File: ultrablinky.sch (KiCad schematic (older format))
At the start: 126 parts, among them J1 DNP, J2 SJ1-3523N, J3 SJ1-3523N, J4 Barrel_Jack_5.5x2.5, J5 DNP, J6 DNP, J7 Terminal5, J8 SJ1-3523N, Q1 DMP6180SK3Q-13, Q2 DMP6180SK3Q-13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

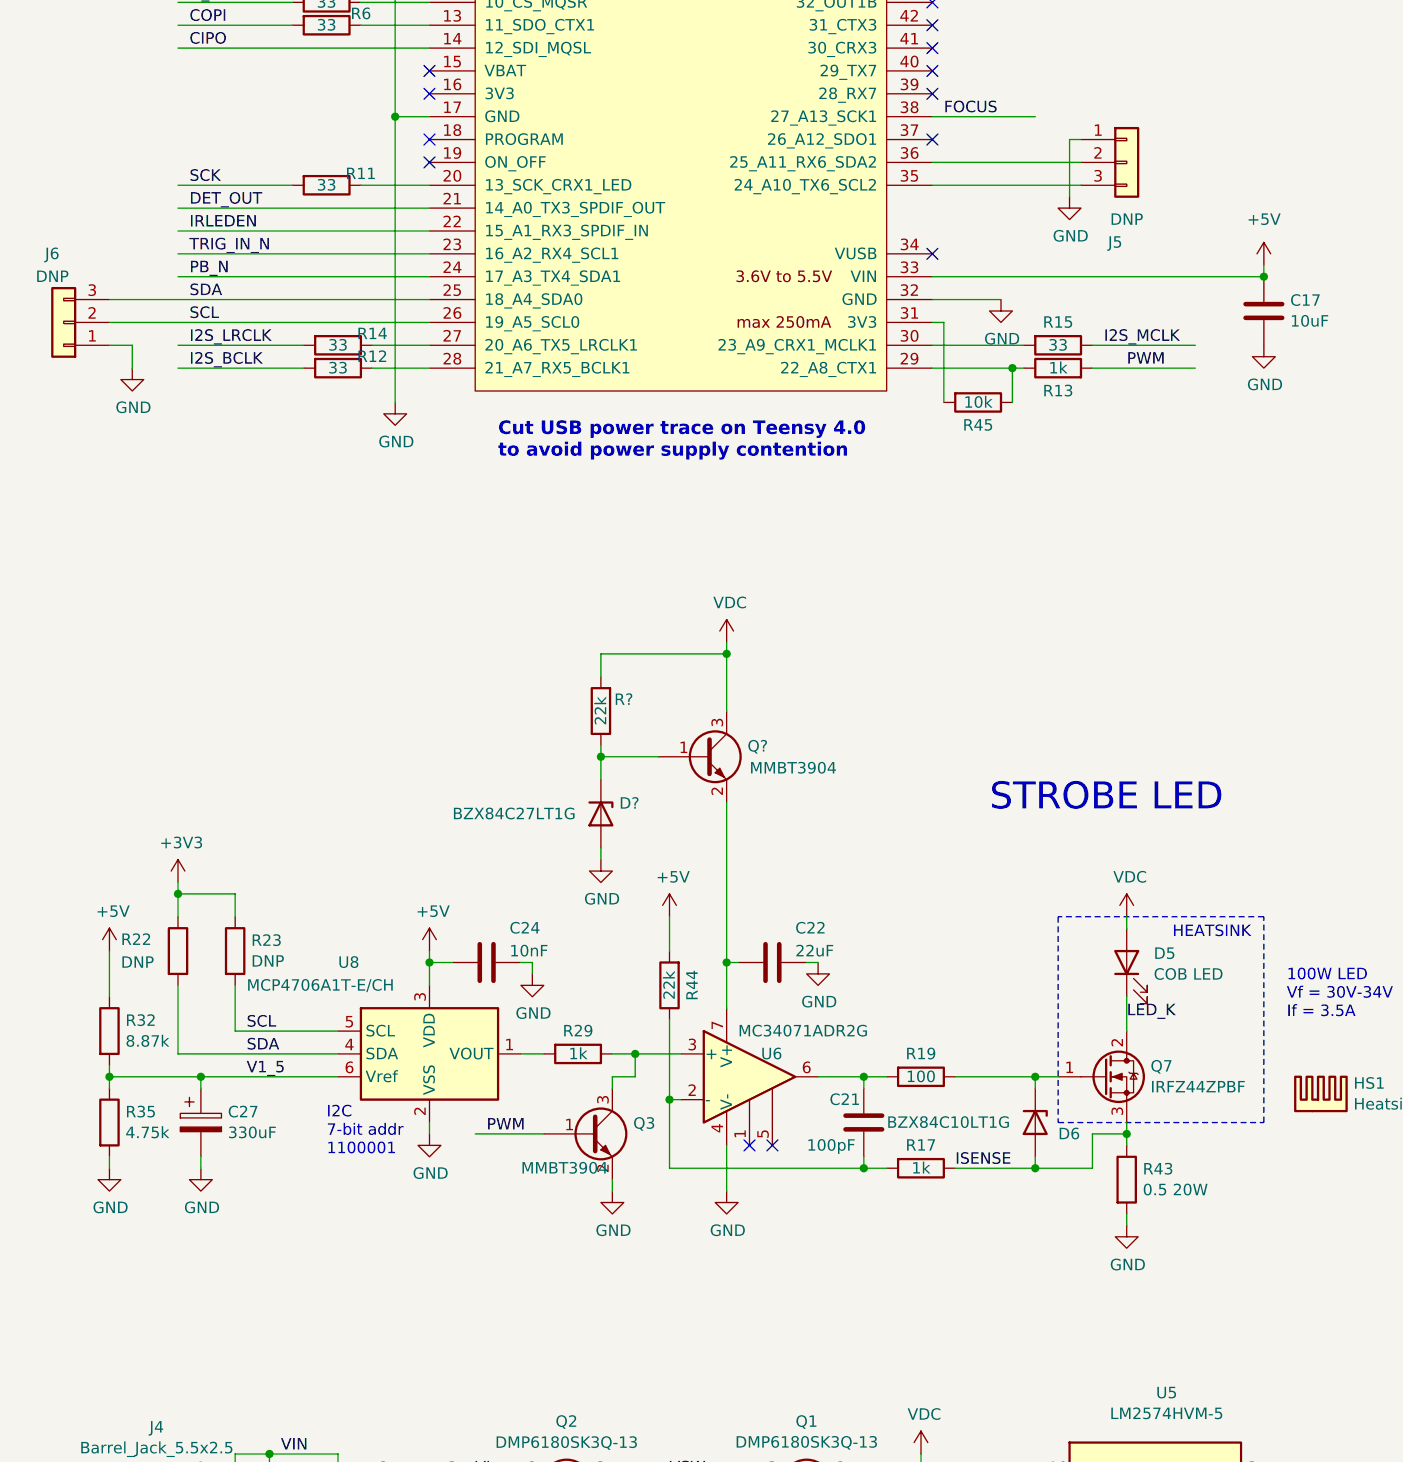
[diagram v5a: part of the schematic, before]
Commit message: Changed current-sense resistor to allow higher current
The current-sense resistor R43 was changed from 0.5-ohm to 0.05-ohm to
allow more current while keeping the voltage across the resistor lower.
Additionally, a pull-down resistor was added to the op amp non-inverting
input so that a current-sense voltage of 0V to 12V gets converted to a
range of 0.2V to 4.9V at the non-inverting input of the op amp.

Additionally, the voltage divider on the Vref input of the MCP4706A DAC
was removed because the VDD power input will be used as the reference
instead.
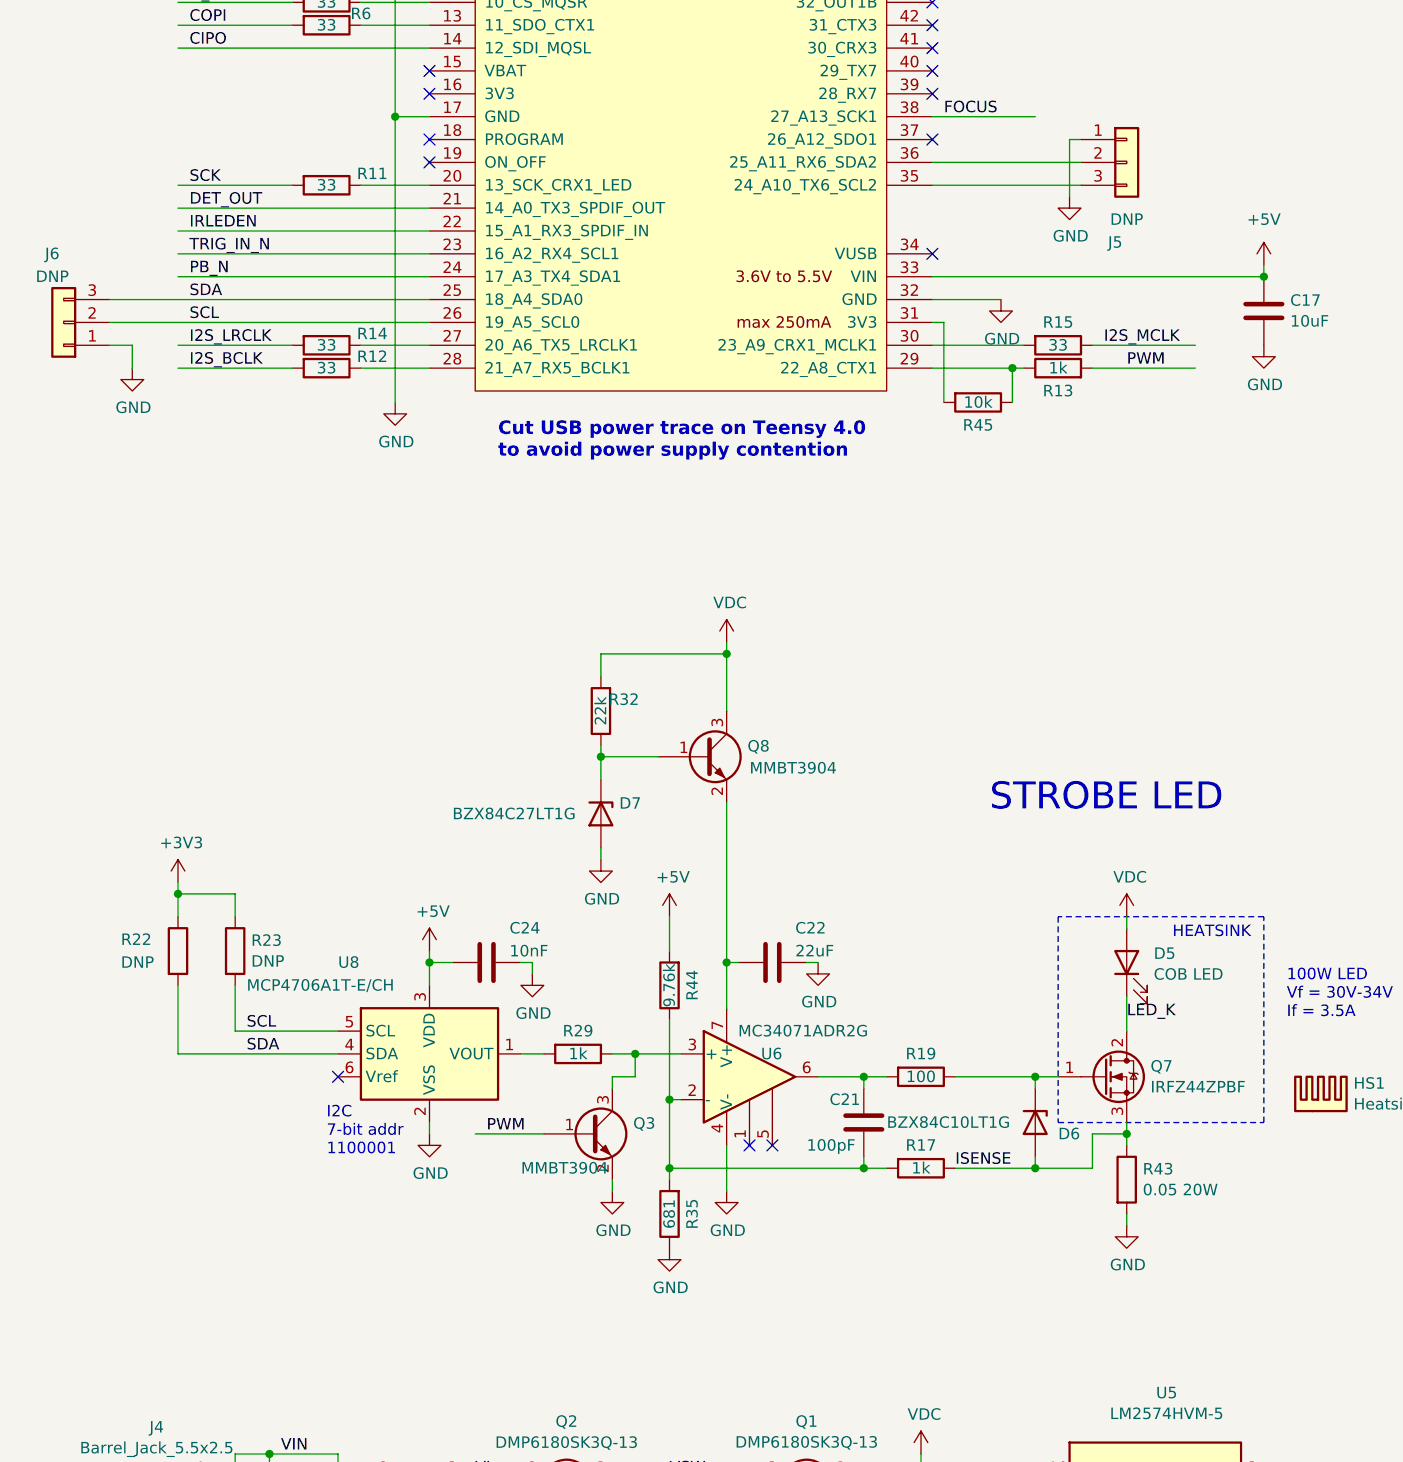
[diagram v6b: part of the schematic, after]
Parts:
- removed C27: 330uF, Capacitor_SMD:CP_Elec_8x10, symbol Device:CP
- removed R32: 8.87k, Resistor_SMD:R_0805_2012Metric, symbol Device:R
- R35: value 4.75k -> 681; Source Mouser 603-RC0805FR-074K75P -> Mouser 603-RC0805FR-07681RL
- R43: value 0.5 20W -> 0.05 20W; Source Mouser 652-PWR220T-20-R500F -> Mouser 652-PWR220T-20-R050J
- R44: value 22k -> 9.76k; Source Mouser 603-RC0805JR-0722KL -> Mouser 603-RC0805FR-079K76L
- gave numbers to parts that had none: 3
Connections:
- net labels removed: V1_5
- wire segments 387 -> 380
- no-connect marks 23 -> 24
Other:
- moved on the sheet: R12, R14
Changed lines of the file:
@@
 P 5450 7200
 F 0 "R43" H 5520 7246 50  0000 L CNN
-F 1 "0.5 20W" H 5520 7155 50  0000 L CNN
+F 1 "0.05 20W" H 5520 7155 50  0000 L CNN
 F 2 "Package_TO_SOT_THT:TO-220-2_Horizontal_TabDown" V 5380 7200 50  0001 C CNN
 F 3 "~" H 5450 7200 50  0001 C CNN
-F 4 "Mouser 652-PWR220T-20-R500F" H 5450 7200 50  0001 C CNN "Source"
+F 4 "Mouser 652-PWR220T-20-R050J" H 5450 7200 50  0001 C CNN "Source"
 	1    5450 7200
 	1    0    0    -1
@@
 Wire Wire Line
 	5750 3650 5300 3650
-Text Label 1600 6750 0    50   ~ 0
-V1_5
 $Comp
 L 0_my_symbols:LM2574HVM-5 U5
@@
 U 1 1 603CBFD5
 P 1950 2850
-F 0 "R11" V 1900 3000 50  0000 C CNN
+F 0 "R11" V 1900 3050 50  0000 C CNN
 F 1 "33" V 1950 2850 50  0000 C CNN
 F 2 "Resistor_SMD:R_0805_2012Metric" V 1880 2850 50  0001 C CNN
@@
 	1    0    0    -1
 $EndComp
-$Comp
-L Device:R R35
-U 1 1 6032F8D7
-P 1000 6950
-F 0 "R35" H 1070 6996 50  0000 L CNN
-F 1 "4.75k" H 1070 6905 50  0000 L CNN
-F 2 "Resistor_SMD:R_0805_2012Metric" V 930 6950 50  0001 C CNN
-F 3 "~" H 1000 6950 50  0001 C CNN
-F 4 "Mouser 603-RC0805FR-074K75P" H 1000 6950 50  0001 C CNN "Source"
-	1    1000 6950
-	1    0    0    -1
-$EndComp
-$Comp
-L Device:R R32
-U 1 1 60330655
-P 1000 6550
-F 0 "R32" H 1070 6596 50  0000 L CNN
-F 1 "8.87k" H 1070 6505 50  0000 L CNN
-F 2 "Resistor_SMD:R_0805_2012Metric" V 930 6550 50  0001 C CNN
-F 3 "~" H 1000 6550 50  0001 C CNN
-F 4 "Mouser 603-RT0805FRE078K87L" H 1000 6550 50  0001 C CNN "Source"
-	1    1000 6550
-	1    0    0    -1
-$EndComp
-$Comp
-L power:GND #PWR0126
-U 1 1 6034CF10
-P 1000 7150
-F 0 "#PWR0126" H 1000 6900 50  0001 C CNN
-F 1 "GND" H 1005 6977 50  0000 C CNN
-F 2 "" H 1000 7150 50  0001 C CNN
-F 3 "" H 1000 7150 50  0001 C CNN
-	1    1000 7150
-	1    0    0    -1
-$EndComp
-Wire Wire Line
-	1000 7100 1000 7150
-Wire Wire Line
-	1000 6800 1000 6750
-Wire Wire Line
-	1000 6700 1000 6750
-Connection ~ 1000 6750
-Wire Wire Line
-	1000 6750 1400 6750
-$Comp
-L power:+5V #PWR0127
-U 1 1 60374662
-P 1000 6200
-F 0 "#PWR0127" H 1000 6050 50  0001 C CNN
-F 1 "+5V" H 1015 6373 50  0000 C CNN
-F 2 "" H 1000 6200 50  0001 C CNN
-F 3 "" H 1000 6200 50  0001 C CNN
-	1    1000 6200
-	1    0    0    -1
-$EndComp
-Wire Wire Line
-	1000 6200 1000 6400
-Wire Wire Line
-	1400 6800 1400 6750
-Connection ~ 1400 6750
-Wire Wire Line
-	1400 6750 2000 6750
-Wire Wire Line
-	1400 7100 1400 7150
-$Comp
-L power:GND #PWR0128
-U 1 1 6039BB5E
-P 1400 7150
-F 0 "#PWR0128" H 1400 6900 50  0001 C CNN
-F 1 "GND" H 1405 6977 50  0000 C CNN
-F 2 "" H 1400 7150 50  0001 C CNN
-F 3 "" H 1400 7150 50  0001 C CNN
-	1    1400 7150
-	1    0    0    -1
-$EndComp
 Text Notes 8000 10350 0    59   ~ 0
 Licensed under CERN-OHL-P v2
@@
 ENCB
 $Comp
-L Device:CP C27
-U 1 1 60454D8D
-P 1400 6950
-F 0 "C27" H 1518 6996 50  0000 L CNN
-F 1 "330uF" H 1518 6905 50  0000 L CNN
-F 2 "Capacitor_SMD:CP_Elec_8x10" H 1438 6800 50  0001 C CNN
-F 3 "~" H 1400 6950 50  0001 C CNN
-F 4 "Mouser 647-UUD1A331MNL" H 1400 6950 50  0001 C CNN "Source"
-	1    1400 6950
-	1    0    0    -1
-$EndComp
-$Comp
 L Device:R R24
 U 1 1 60484532
@@
 	1300 1750 1800 1750
 Wire Wire Line
-	1300 3650 1850 3650
+	1300 3650 1800 3650
 Wire Wire Line
-	1300 3550 1850 3550
+	1300 3550 1800 3550
 Wire Wire Line
 	4600 3550 5000 3550
@@
 L Device:R R12
 U 1 1 60B12468
-P 2000 3650
-F 0 "R12" V 1950 3800 50  0000 C CNN
-F 1 "33" V 2000 3650 50  0000 C CNN
-F 2 "Resistor_SMD:R_0805_2012Metric" V 1930 3650 50  0001 C CNN
-F 3 "~" H 2000 3650 50  0001 C CNN
-F 4 "Mouser 603-RC0805JR-1333RL" H 2000 3650 50  0001 C CNN "Source"
-	1    2000 3650
+P 1950 3650
+F 0 "R12" V 1900 3850 50  0000 C CNN
+F 1 "33" V 1950 3650 50  0000 C CNN
+F 2 "Resistor_SMD:R_0805_2012Metric" V 1880 3650 50  0001 C CNN
+F 3 "~" H 1950 3650 50  0001 C CNN
+F 4 "Mouser 603-RC0805JR-1333RL" H 1950 3650 50  0001 C CNN "Source"
+	1    1950 3650
 	0    1    1    0
 $EndComp
 Wire Wire Line
-	2150 3650 2400 3650
+	2100 3650 2400 3650
 $Comp
 L Device:R R14
 U 1 1 60B12D4F
-P 2000 3550
-F 0 "R14" V 1950 3700 50  0000 C CNN
-F 1 "33" V 2000 3550 50  0000 C CNN
-F 2 "Resistor_SMD:R_0805_2012Metric" V 1930 3550 50  0001 C CNN
-F 3 "~" H 2000 3550 50  0001 C CNN
-F 4 "Mouser 603-RC0805JR-1333RL" H 2000 3550 50  0001 C CNN "Source"
-	1    2000 3550
+P 1950 3550
+F 0 "R14" V 1900 3750 50  0000 C CNN
+F 1 "33" V 1950 3550 50  0000 C CNN
+F 2 "Resistor_SMD:R_0805_2012Metric" V 1880 3550 50  0001 C CNN
+F 3 "~" H 1950 3550 50  0001 C CNN
+F 4 "Mouser 603-RC0805JR-1333RL" H 1950 3550 50  0001 C CNN "Source"
+	1    1950 3550
 	0    1    1    0
 $EndComp
 Wire Wire Line
-	2150 3550 2400 3550
+	2100 3550 2400 3550
 Text Notes 11900 8500 0    50   ~ 0
 I2C\n7-bit addr\n0001010
@@
 P 3450 6350
 F 0 "R44" V 3350 6350 50  0000 C CNN
-F 1 "22k" V 3450 6350 50  0000 C CNN
+F 1 "9.76k" V 3450 6350 50  0000 C CNN
 F 2 "Resistor_SMD:R_0805_2012Metric" V 3380 6350 50  0001 C CNN
 F 3 "~" H 3450 6350 50  0001 C CNN
-F 4 "Mouser 603-RC0805JR-0722KL" H 3450 6350 50  0001 C CNN "Source"
+F 4 "Mouser 603-RC0805FR-079K76L" H 3450 6350 50  0001 C CNN "Source"
 	1    3450 6350
 	-1   0    0    1
@@
 	3450 6050 3450 6200
 $Comp
-L power:VDC #PWR?
+L power:VDC #PWR05
 U 1 1 6106C1A4
 P 4550 8400
-F 0 "#PWR?" H 4550 8300 50  0001 C CNN
+F 0 "#PWR05" H 4550 8300 50  0001 C CNN
 F 1 "VDC" H 4565 8573 50  0000 C CNN
 F 2 "" H 4550 8400 50  0001 C CNN
@@
 $EndComp
 $Comp
-L power:VDC #PWR?
+L power:VDC #PWR06
 U 1 1 6107AF6A
 P 5450 6050
-F 0 "#PWR?" H 5450 5950 50  0001 C CNN
+F 0 "#PWR06" H 5450 5950 50  0001 C CNN
 F 1 "VDC" H 5465 6223 50  0000 C CNN
 F 2 "" H 5450 6050 50  0001 C CNN
@@
 $EndComp
 $Comp
-L Transistor_BJT:MMBT3904 Q?
+L Transistor_BJT:MMBT3904 Q8
 U 1 1 6108F88A
 P 3600 5350
-F 0 "Q?" H 3791 5396 50  0000 L CNN
+F 0 "Q8" H 3791 5396 50  0000 L CNN
 F 1 "MMBT3904" H 3800 5300 50  0000 L CNN
 F 2 "Package_TO_SOT_SMD:SOT-23" H 3800 5275 50  0001 L CIN
@@
 	4700 6750 5050 6750
 $Comp
-L power:GND #PWR?
+L power:GND #PWR02
 U 1 1 610CE73D
 P 3150 5800
-F 0 "#PWR?" H 3150 5550 50  0001 C CNN
+F 0 "#PWR02" H 3150 5550 50  0001 C CNN
 F 1 "GND" H 3155 5627 50  0000 C CNN
 F 2 "" H 3150 5800 50  0001 C CNN
@@
 	3150 5350 3400 5350
 $Comp
-L power:VDC #PWR?
+L power:VDC #PWR04
 U 1 1 6114E880
 P 3700 4850
-F 0 "#PWR?" H 3700 4750 50  0001 C CNN
+F 0 "#PWR04" H 3700 4750 50  0001 C CNN
 F 1 "VDC" H 3715 5023 50  0000 C CNN
 F 2 "" H 3700 4850 50  0001 C CNN
@@
 	5050 7150 5300 7150
 $Comp
-L Diode:BZX84Cxx D?
+L Diode:BZX84Cxx D7
 U 1 1 612A00AB
 P 3150 5600
-F 0 "D?" V 3104 5680 50  0000 L CNN
+F 0 "D7" V 3104 5680 50  0000 L CNN
 F 1 "BZX84C27LT1G " V 3150 4950 50  0000 L CNN
 F 2 "Diode_SMD:D_SOT-23_ANK" H 3150 5425 50  0001 C CNN
@@
 $EndComp
 $Comp
-L Device:R R?
+L Device:R R32
 U 1 1 612C6BB1
 P 3150 5150
-F 0 "R?" H 3050 5100 50  0000 C CNN
+F 0 "R32" H 3050 5100 50  0000 C CNN
 F 1 "22k" V 3150 5150 50  0000 C CNN
 F 2 "Resistor_SMD:R_0805_2012Metric" V 3080 5150 50  0001 C CNN
@@
 	-1   0    0    1
 $EndComp
+$Comp
+L Device:R R35
+U 1 1 61473BCB
+P 3450 7350
+F 0 "R35" V 3350 7350 50  0000 C CNN
+F 1 "681" V 3450 7350 50  0000 C CNN
+F 2 "Resistor_SMD:R_0805_2012Metric" V 3380 7350 50  0001 C CNN
+F 3 "~" H 3450 7350 50  0001 C CNN
+F 4 "Mouser 603-RC0805FR-07681RL" H 3450 7350 50  0001 C CNN "Source"
+	1    3450 7350
+	-1   0    0    1
+$EndComp
+Wire Wire Line
+	3450 7200 3450 7150
+Connection ~ 3450 7150
+$Comp
+L power:GND #PWR03
+U 1 1 6149F8FA
+P 3450 7500
+F 0 "#PWR03" H 3450 7250 50  0001 C CNN
+F 1 "GND" H 3455 7327 50  0000 C CNN
+F 2 "" H 3450 7500 50  0001 C CNN
+F 3 "" H 3450 7500 50  0001 C CNN
+	1    3450 7500
+	1    0    0    -1
+$EndComp
+NoConn ~ 2000 6750
 $EndSCHEMATC
